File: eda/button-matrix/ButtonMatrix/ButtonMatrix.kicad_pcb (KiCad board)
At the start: 2 copper layers, 191.5 x 87.2 mm, 18 parts, among them SW1 SW_Omron_B3FS, SW10 SW_Omron_B3FS, SW11 SW_Omron_B3FS, SW12 SW_Omron_B3FS, SW13 SW_Omron_B3FS, SW14 SW_Omron_B3FS, SW15 SW_Omron_B3FS, SW16 SW_Omron_B3FS, SW2 SW_Omron_B3FS, SW3 SW_Omron_B3FS, SW4 SW_Omron_B3FS, SW5 SW_Omron_B3FS, SW6 SW_Omron_B3FS, SW7 SW_Omron_B3FS, SW8 SW_Omron_B3FS, SW9 SW_Omron_B3FS

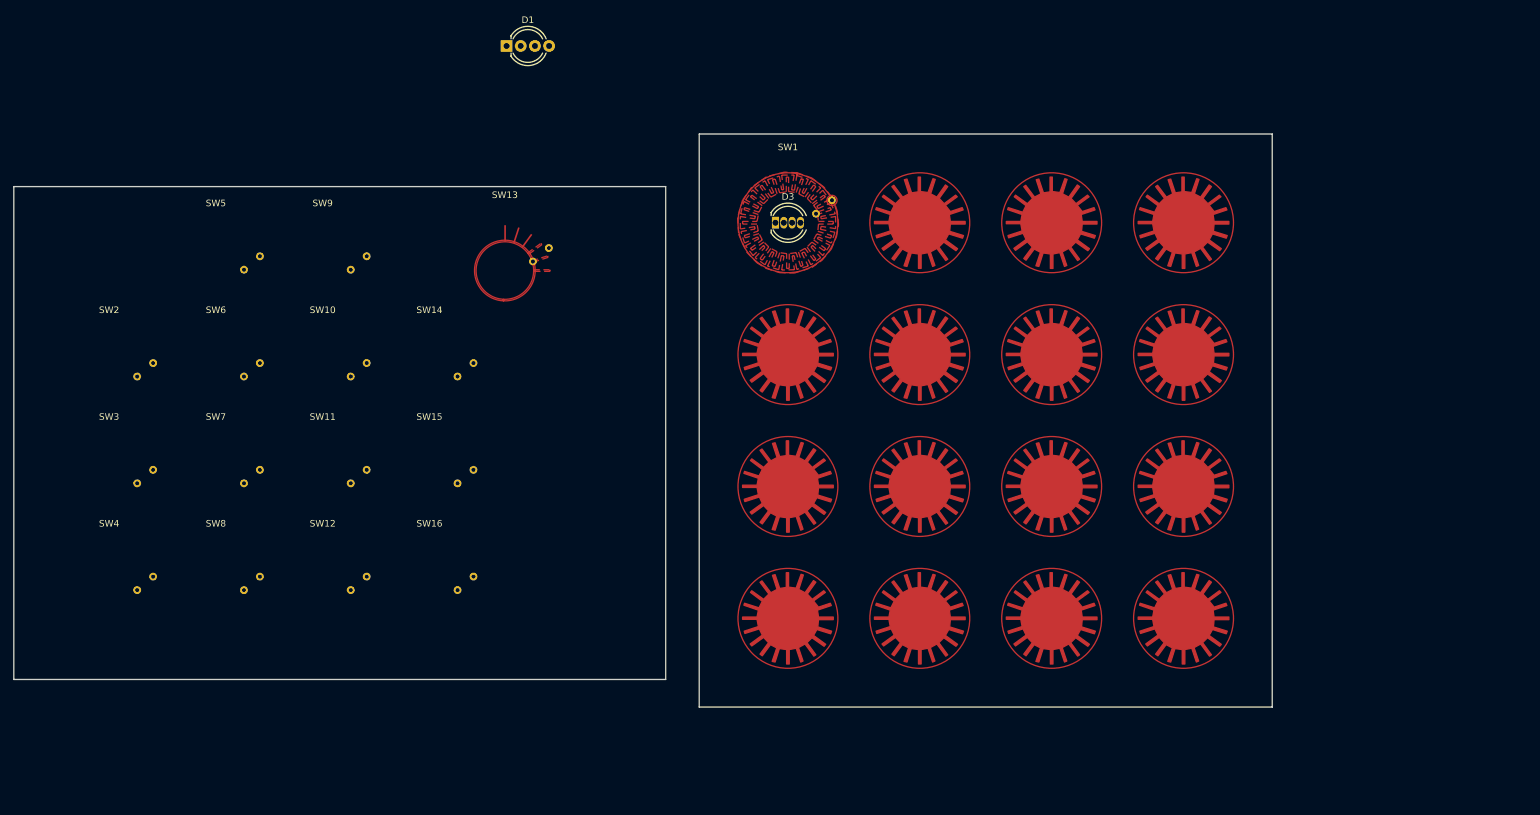
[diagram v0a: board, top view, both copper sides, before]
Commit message: - Updated mesh button connections
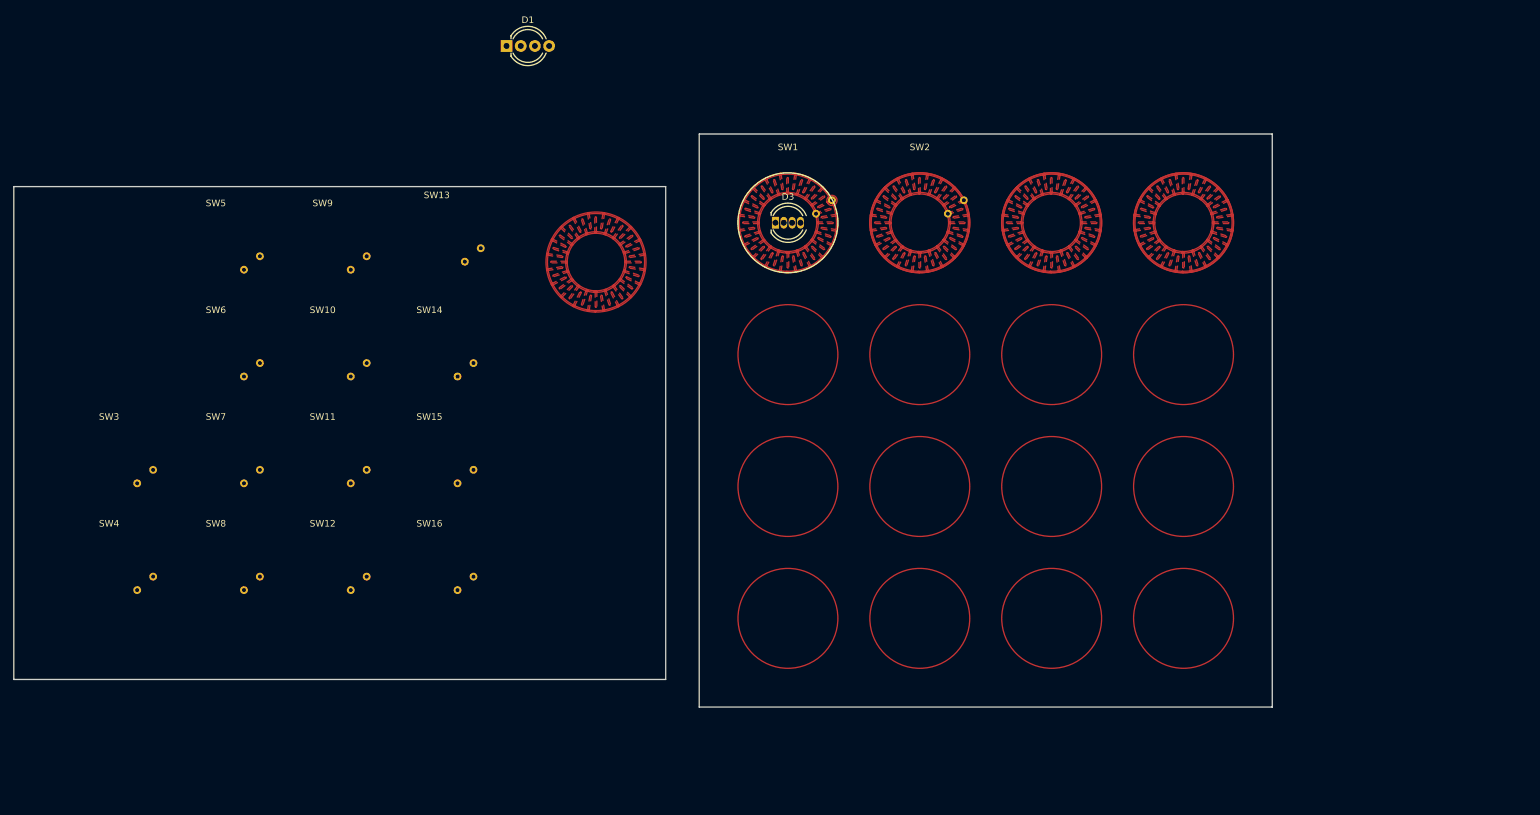
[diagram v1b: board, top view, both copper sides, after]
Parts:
- moved SW2 125.8 mm to (161.6, 72.9)
- moved SW13 10.4 mm to (88.1, 80.2)
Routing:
- removed copper zone on F.Cu, net unconnected-(SW1-Pad1)

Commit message: - Updated the pcb for the new 4x4 button matrix - Added support imgui and desktop support
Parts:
- added D10: 1N4148, Diode_THT:D_DO-35_SOD27_P7.62mm_Horizontal, F.Cu at (228.9, 106.8)
- added D11: 1N4148, Diode_THT:D_DO-35_SOD27_P7.62mm_Horizontal, F.Cu at (228.9, 110.3)
- added D12: 1N4148, Diode_THT:D_DO-35_SOD27_P7.62mm_Horizontal, F.Cu at (228.9, 113.9)
- added D13: 1N4148, Diode_THT:D_DO-35_SOD27_P7.62mm_Horizontal, B.Cu at (145.3, 143.8)
- added D14: 1N4148, Diode_THT:D_DO-35_SOD27_P7.62mm_Horizontal, F.Cu at (228.9, 121.0)
- added D15: 1N4148, Diode_THT:D_DO-35_SOD27_P7.62mm_Horizontal, F.Cu at (228.9, 124.5)
- added D16: 1N4148, Diode_THT:D_DO-35_SOD27_P7.62mm_Horizontal, F.Cu at (228.9, 128.1)
- added D17: LED_RGBA, LED_THT:LED_D5.0mm-4_RGB, F.Cu at (139.6, 72.9)
- added D18: LED_RGBA, LED_THT:LED_D5.0mm-4_RGB_Wide_Pins, F.Cu at (68.4, 58.1)
- added D2: 1N4148, Diode_THT:D_DO-35_SOD27_P7.62mm_Horizontal, F.Cu at (221.7, 68.8)
- added D4: 1N4148, Diode_THT:D_DO-35_SOD27_P7.62mm_Horizontal, F.Cu at (228.9, 85.5)
- added D5: 1N4148, Diode_THT:D_DO-35_SOD27_P7.62mm_Horizontal, B.Cu at (145.3, 103.0)
- added D6: 1N4148, Diode_THT:D_DO-35_SOD27_P7.62mm_Horizontal, F.Cu at (228.9, 92.6)
- added D7: 1N4148, Diode_THT:D_DO-35_SOD27_P7.62mm_Horizontal, F.Cu at (228.9, 96.1)
- added D8: 1N4148, Diode_THT:D_DO-35_SOD27_P7.62mm_Horizontal, F.Cu at (228.9, 99.7)
- added D9: 1N4148, Diode_THT:D_DO-35_SOD27_P7.62mm_Horizontal, B.Cu at (145.3, 123.1)
- D1: value LED_RGBA -> 1N4148; footprint LED_THT:LED_D5.0mm-4_RGB_Wide_Pins -> Diode_THT:D_DO-35_SOD27_P7.62mm_Horizontal; moved to B.Cu
- D3: value LED_RGBA -> 1N4148; footprint LED_THT:LED_D5.0mm-4_RGB -> Diode_THT:D_DO-35_SOD27_P7.62mm_Horizontal
- moved SW4 173.2 mm to (201.7, 72.9)
- moved SW8 151.9 mm to (201.7, 93.0)
- moved SW3 149.2 mm to (181.6, 72.9)
- moved SW12 132.1 mm to (201.7, 113.0)
- moved SW7 128.9 mm to (181.6, 93.0)
- moved SW16 114.8 mm to (201.7, 133.1)
- moved SW11 110.9 mm to (181.6, 113.0)
- moved SW6 107.2 mm to (161.6, 93.0)
- moved SW15 96.6 mm to (181.6, 133.1)
- moved SW10 92.2 mm to (161.6, 113.0)
- moved D3 89.8 mm to (228.9, 81.9)
- moved SW5 87.8 mm to (141.5, 93.0)
- moved SW14 82.6 mm to (161.6, 133.1)
- moved SW9 77.5 mm to (141.5, 113.0)
- moved SW13 75.2 mm to (141.5, 133.1)
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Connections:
- D1 pad 1: unconnected-(D1-RK-Pad1) -> /SW_COL1
- D1 pad 2: unconnected-(D1-GK-Pad2) -> Net-(D1-A)
- D3 pad 1: unconnected-(D3-RK-Pad1) -> /SW_COL3
- D3 pad 2: unconnected-(D3-GK-Pad2) -> Net-(D3-A)
- SW1 pad 1: unconnected-(SW1-Pad1) -> /SW_ROW1
- SW1 pad 2: Net-(SW1-Pad2) -> Net-(D1-A)
- SW10 pad 1: Net-(SW1-Pad2) -> /SW_ROW3
- SW10 pad 2: Net-(SW10-Pad2) -> Net-(D10-A)
- SW11 pad 1: Net-(SW10-Pad2) -> /SW_ROW3
- SW11 pad 2: Net-(SW11-Pad2) -> Net-(D11-A)
- SW12 pad 1: Net-(SW11-Pad2) -> /SW_ROW3
- SW12 pad 2: Net-(SW12-Pad2) -> Net-(D12-A)
- SW13 pad 1: unconnected-(SW13-Pad1) -> /SW_ROW4
- SW13 pad 2: Net-(SW1-Pad2) -> Net-(D13-A)
- SW14 pad 1: Net-(SW1-Pad2) -> /SW_ROW4
- SW14 pad 2: Net-(SW10-Pad2) -> Net-(D14-A)
- SW15 pad 1: Net-(SW10-Pad2) -> /SW_ROW4
- SW15 pad 2: Net-(SW11-Pad2) -> Net-(D15-A)
- SW16 pad 1: Net-(SW11-Pad2) -> /SW_ROW4
- SW16 pad 2: Net-(SW12-Pad2) -> Net-(D16-A)
- SW2 pad 1: Net-(SW1-Pad2) -> /SW_ROW1
- SW2 pad 2: Net-(SW10-Pad2) -> Net-(D2-A)
- SW3 pad 1: Net-(SW10-Pad2) -> /SW_ROW1
- SW3 pad 2: Net-(SW11-Pad2) -> Net-(D3-A)
- SW4 pad 1: Net-(SW11-Pad2) -> /SW_ROW1
- SW4 pad 2: Net-(SW12-Pad2) -> Net-(D4-A)
- SW5 pad 1: unconnected-(SW5-Pad1) -> /SW_ROW2
- SW5 pad 2: Net-(SW1-Pad2) -> Net-(D5-A)
- SW6 pad 1: Net-(SW1-Pad2) -> /SW_ROW2
- SW6 pad 2: Net-(SW10-Pad2) -> Net-(D6-A)
- SW7 pad 1: Net-(SW10-Pad2) -> /SW_ROW2
- SW7 pad 2: Net-(SW11-Pad2) -> Net-(D7-A)
- SW8 pad 1: Net-(SW11-Pad2) -> /SW_ROW2
- SW8 pad 2: Net-(SW12-Pad2) -> Net-(D8-A)
- SW9 pad 1: unconnected-(SW9-Pad1) -> /SW_ROW3
- SW9 pad 2: Net-(SW1-Pad2) -> Net-(D9-A)
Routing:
- net /SW_COL1: track 0.00 -> 79.3 mm
- net /SW_ROW4: track 0.00 -> 60.2 mm
- net /SW_ROW3: track 0.00 -> 60.2 mm
- net /SW_ROW2: track 0.00 -> 60.2 mm
- net /SW_ROW1: track 0.00 -> 60.2 mm
- net Net-(D9-A): track 0.00 -> 26.7 mm
- net Net-(D5-A): track 0.00 -> 24.8 mm
- net Net-(D1-A): track 0.00 -> 24.8 mm
- net Net-(D13-A): track 0.00 -> 24.7 mm
- added copper zone on F.Cu, net /SW_ROW1
- added copper zone on F.Cu, net /SW_ROW2
- added copper zone on F.Cu, net /SW_ROW3
- added copper zone on F.Cu, net /SW_ROW4
- added copper zone on F.Cu, net Net-(D1-A)
- added copper zone on F.Cu, net Net-(D10-A)
- added copper zone on F.Cu, net Net-(D11-A)
- added copper zone on F.Cu, net Net-(D12-A)
- added copper zone on F.Cu, net Net-(D13-A)
- added copper zone on F.Cu, net Net-(D14-A)
- added copper zone on F.Cu, net Net-(D15-A)
- added copper zone on F.Cu, net Net-(D16-A)
- added copper zone on F.Cu, net Net-(D2-A)
- added copper zone on F.Cu, net Net-(D3-A)
- added copper zone on F.Cu, net Net-(D4-A)
- added copper zone on F.Cu, net Net-(D5-A)
- added copper zone on F.Cu, net Net-(D6-A)
- added copper zone on F.Cu, net Net-(D7-A)
- added copper zone on F.Cu, net Net-(D8-A)
- added copper zone on F.Cu, net Net-(D9-A)
- removed copper zone on F.Cu, net Net-(SW1-Pad2)
- removed copper zone on F.Cu, net unconnected-(SW13-Pad1)
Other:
- board size 191.5 x 87.2 mm -> 87.2 x 87.2 mm

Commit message: - Updates to button matrix pcb
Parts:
- D10, D11, D12, D14, D15, D16, D2, D3, D4, D6, D7, D8: moved to B.Cu
- moved D14 74.7 mm to (157.8, 143.8)
- moved D10 73.0 mm to (157.8, 123.1)
- moved D6 71.9 mm to (157.8, 103.0)
- moved D2 65.5 mm to (157.8, 82.9)
- moved D15 54.6 mm to (177.8, 143.8)
- moved D11 52.7 mm to (177.8, 123.1)
- moved D7 51.6 mm to (177.8, 103.0)
- moved D3 51.1 mm to (177.8, 82.9)
- moved D16 34.8 mm to (197.9, 143.8)
- moved D12 32.4 mm to (197.9, 123.1)
- moved D8 31.2 mm to (197.9, 103.0)
- moved D4 31.1 mm to (197.9, 82.9)
- moved D1 7.62 mm to (137.7, 82.9), turned to 0 degrees
- moved D13 7.62 mm to (137.7, 143.8), turned to 0 degrees
- moved D5 7.62 mm to (137.7, 103.0), turned to 0 degrees
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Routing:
- net /SW_COL1: track 79.3 -> 0.00 mm
- net Net-(D9-A): track 26.7 -> 0.00 mm
- net Net-(D5-A): track 24.8 -> 0.00 mm
- net Net-(D1-A): track 24.8 -> 0.00 mm
- net Net-(D13-A): track 24.7 -> 0.00 mm

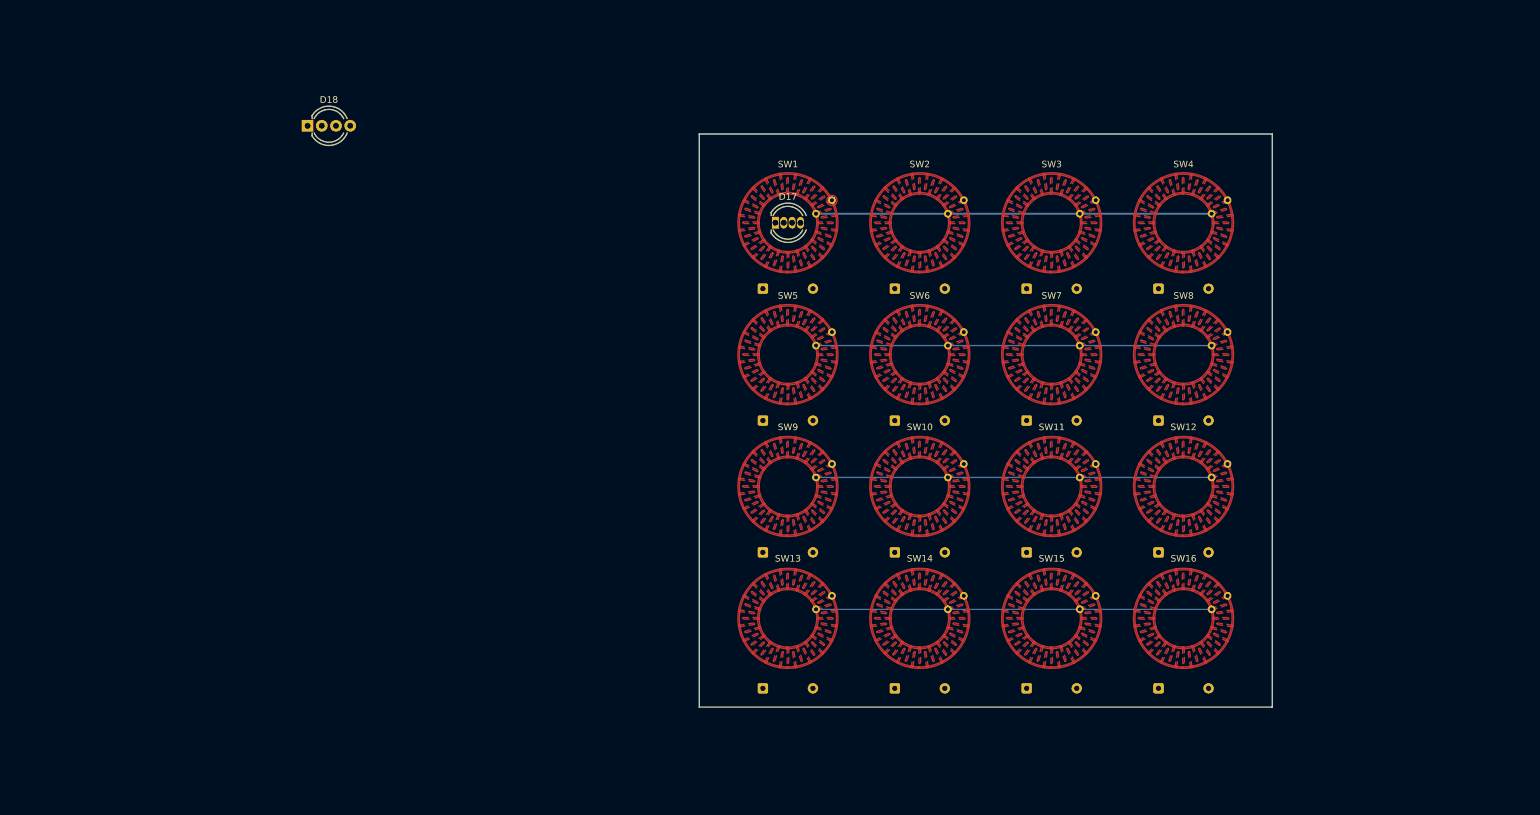
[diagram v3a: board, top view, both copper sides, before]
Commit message: - Added m2 mounting holes to the pcb
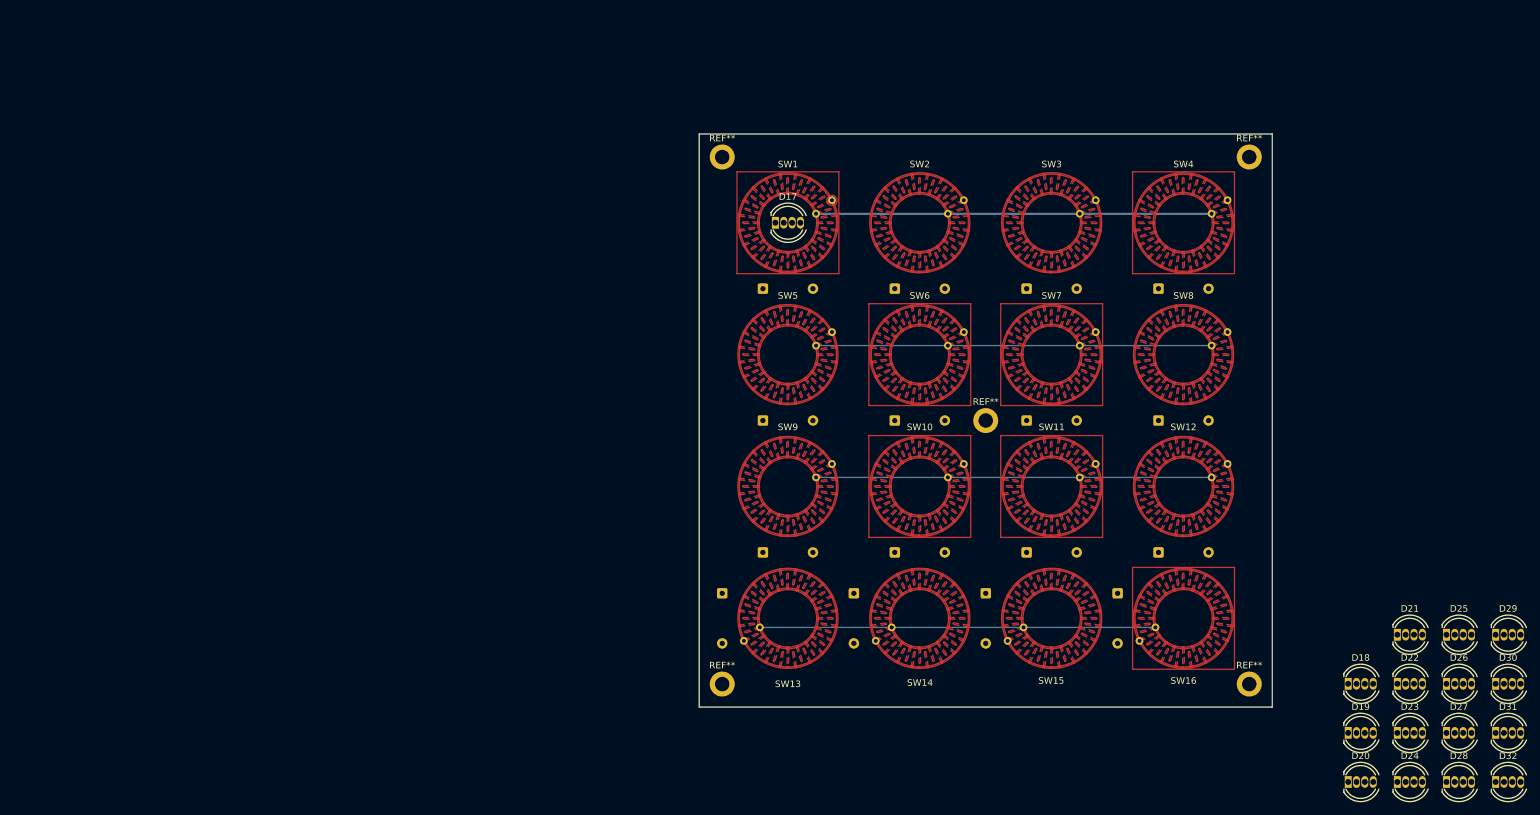
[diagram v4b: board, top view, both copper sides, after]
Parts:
- added D19: LED_BGAR, LED_THT:LED_D5.0mm-4_RGB, F.Cu at (226.8, 150.5)
- added D20: LED_BGAR, LED_THT:LED_D5.0mm-4_RGB, F.Cu at (226.8, 158.0)
- added D21: LED_BGAR, LED_THT:LED_D5.0mm-4_RGB, F.Cu at (234.2, 135.6)
- added D22: LED_BGAR, LED_THT:LED_D5.0mm-4_RGB, F.Cu at (234.2, 143.1)
- added D23: LED_BGAR, LED_THT:LED_D5.0mm-4_RGB, F.Cu at (234.2, 150.5)
- added D24: LED_BGAR, LED_THT:LED_D5.0mm-4_RGB, F.Cu at (234.2, 158.0)
- added D25: LED_BGAR, LED_THT:LED_D5.0mm-4_RGB, F.Cu at (241.7, 135.6)
- added D26: LED_BGAR, LED_THT:LED_D5.0mm-4_RGB, F.Cu at (241.7, 143.1)
- added D27: LED_BGAR, LED_THT:LED_D5.0mm-4_RGB, F.Cu at (241.7, 150.5)
- added D28: LED_BGAR, LED_THT:LED_D5.0mm-4_RGB, F.Cu at (241.7, 158.0)
- added D29: LED_BGAR, LED_THT:LED_D5.0mm-4_RGB, F.Cu at (249.2, 135.6)
- added D30: LED_BGAR, LED_THT:LED_D5.0mm-4_RGB, F.Cu at (249.2, 143.1)
- added D31: LED_BGAR, LED_THT:LED_D5.0mm-4_RGB, F.Cu at (249.2, 150.5)
- added D32: LED_BGAR, LED_THT:LED_D5.0mm-4_RGB, F.Cu at (249.2, 158.0)
- added REF**: MountingHole_2.2mm_M2_ISO14580_Pad, MountingHole:MountingHole_2.2mm_M2_ISO14580_Pad, F.Cu at (131.5, 62.9)
- added REF**: MountingHole_2.2mm_M2_ISO14580_Pad, MountingHole:MountingHole_2.2mm_M2_ISO14580_Pad, F.Cu at (211.7, 143.1)
- added REF**: MountingHole_2.2mm_M2_ISO14580_Pad, MountingHole:MountingHole_2.2mm_M2_ISO14580_Pad, F.Cu at (131.5, 143.1)
- added REF**: MountingHole_2.2mm_M2_ISO14580_Pad, MountingHole:MountingHole_2.2mm_M2_ISO14580_Pad, F.Cu at (171.6, 103.0)
- added REF**: MountingHole_2.2mm_M2_ISO14580_Pad, MountingHole:MountingHole_2.2mm_M2_ISO14580_Pad, F.Cu at (211.7, 62.9)
- D17: value LED_RGBA -> LED_BGAR
- D18: value LED_RGBA -> LED_BGAR; footprint LED_THT:LED_D5.0mm-4_RGB_Wide_Pins -> LED_THT:LED_D5.0mm-4_RGB
- moved D18 179.7 mm to (226.8, 143.1)
- moved D16 15.7 mm to (191.7, 129.3), turned to -90 degrees
- moved D14 15.7 mm to (151.5, 129.3), turned to -90 degrees
- moved D15 15.7 mm to (171.6, 129.3), turned to -90 degrees
- moved D13 15.7 mm to (131.5, 129.3), turned to -90 degrees
- turned SW13 to 180 degrees
- turned SW14 to 180 degrees
- turned SW15 to 180 degrees
- turned SW16 to 180 degrees
